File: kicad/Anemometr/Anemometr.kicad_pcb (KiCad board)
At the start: 2 copper layers, 31.8 x 26.7 mm, 74 parts, among them J1 Conn_01x01_Female, J10 Z3, J11 Z3, J12 Z4, J13 Z4, J14 SWD, J15 SWC, J16 +12v, J17 GND, J2 Conn_01x01_Female, J3 RST, J4 TxD, J5 RxD, J6 Z1, J7 Z1, J8 Z2, J9 Z2, U1 TS5A3166DBVR, U2 LMV7239, U3 TS5A3166DBVR, U4 TS5A3166DBVR, U5 STM32F103C8Tx, U6 TS5A3166DBVR, U7 LM2734Y, U8 MCP1700-5002E_SOT23, U9 MCP1700-3002E_SOT23, Y1 8MHz

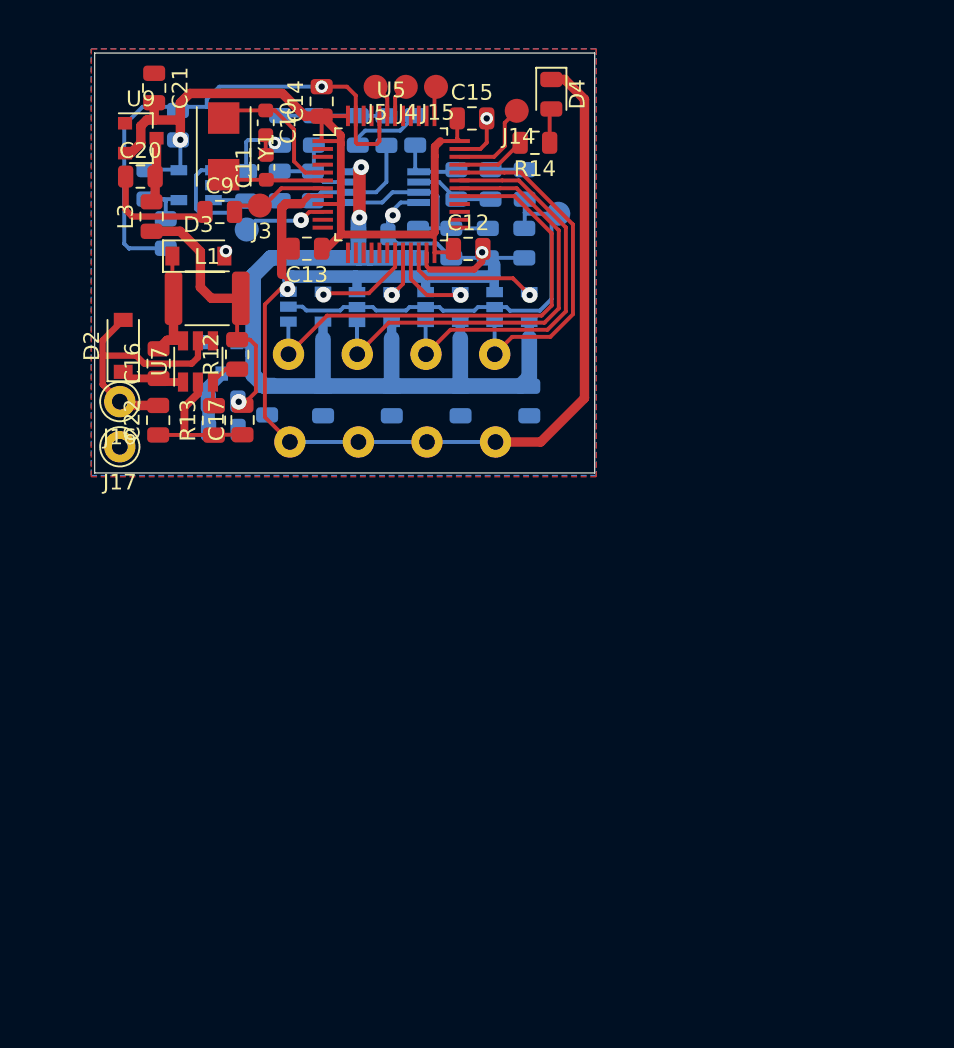
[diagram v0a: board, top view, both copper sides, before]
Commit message: изменено:      kicad/Anemometr/Anemometr-cache.lib 	изменено:      kicad/Anemometr/Anemometr.kicad_pcb 	изменено:      kicad/Anemometr/Anemometr.kicad_pcb-bak 	изменено:      kicad/Anemometr/Anemometr.sch 	изменено:      kicad/Anemometr/Anemometr.sch-bak 	изменено:      kicad/Anemometr/fp-info-cache
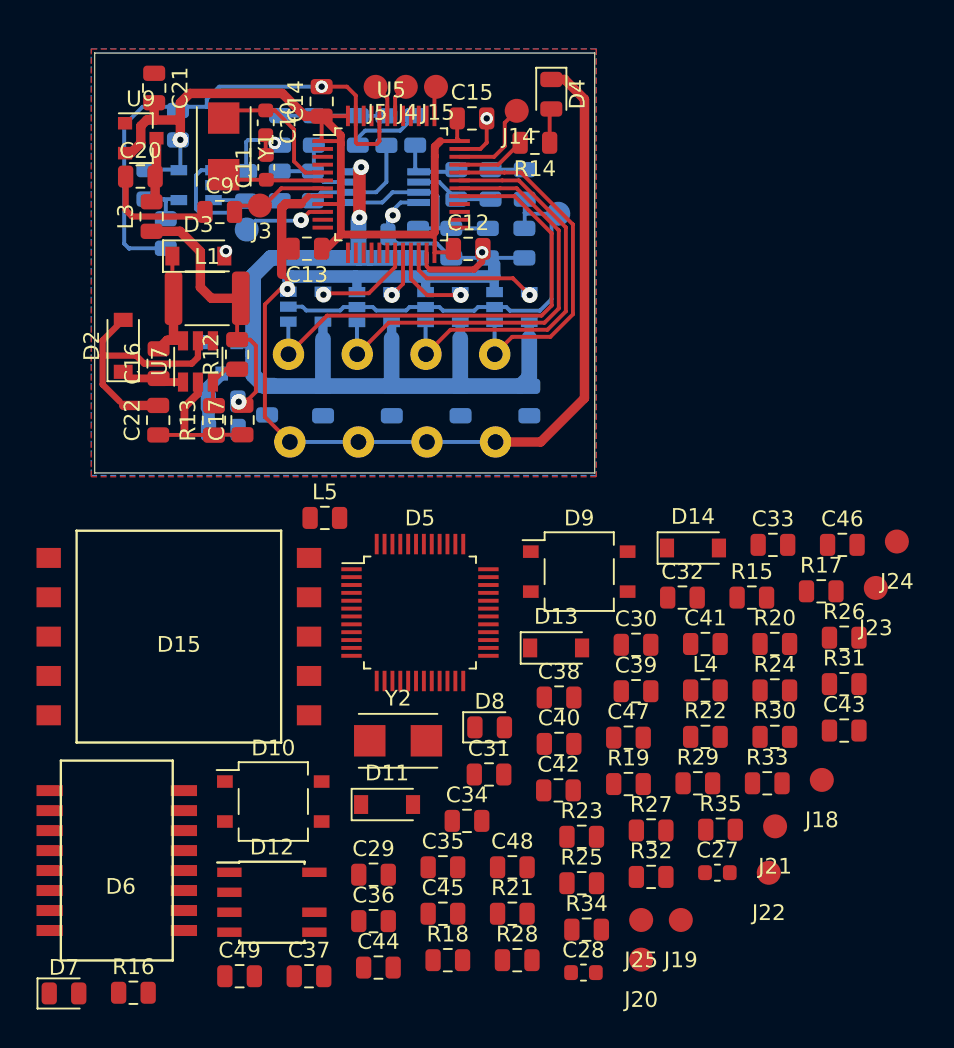
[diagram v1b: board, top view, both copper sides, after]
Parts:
- removed J16: +12v, Connector_Pin:Pin_D1.0mm_L10.0mm
- removed J17: GND, Connector_Pin:Pin_D1.0mm_L10.0mm
- added C27: 10p, Capacitor_SMD:C_0603_1608Metric, F.Cu at (62.4, 113.0)
- added C28: 10p, Capacitor_SMD:C_0603_1608Metric, F.Cu at (53.9, 119.4)
- added C29: 10uF, Capacitor_SMD:C_0805_2012Metric, F.Cu at (40.6, 113.2)
- added C30: 10uF, Capacitor_SMD:C_0805_2012Metric, F.Cu at (57.3, 98.5)
- added C31: 10nF, Capacitor_SMD:C_0805_2012Metric, F.Cu at (47.9, 106.8)
- added C32: 22nF, Capacitor_SMD:C_0805_2012Metric, F.Cu at (60.2, 95.5)
- added C33: 6.8nF, Capacitor_SMD:C_0805_2012Metric, F.Cu at (66.0, 92.2)
- added C34: 6.8nF, Capacitor_SMD:C_0805_2012Metric, F.Cu at (46.5, 109.7)
- added C35: 4.7nF/2kV, Capacitor_SMD:C_0805_2012Metric, F.Cu at (45.0, 112.7)
- added C36: 0.1uF, Capacitor_SMD:C_0805_2012Metric, F.Cu at (40.6, 116.1)
- added C37: 10uF, Capacitor_SMD:C_0805_2012Metric, F.Cu at (36.5, 119.6)
- added C38: 0.1uF, Capacitor_SMD:C_0805_2012Metric, F.Cu at (52.4, 101.9)
- added C39: 0.1uF, Capacitor_SMD:C_0805_2012Metric, F.Cu at (57.3, 101.5)
- added C40: 0.1uF, Capacitor_SMD:C_0805_2012Metric, F.Cu at (52.4, 104.8)
- added C41: 0.1uF, Capacitor_SMD:C_0805_2012Metric, F.Cu at (61.7, 98.5)
- added C42: 0.1uF, Capacitor_SMD:C_0805_2012Metric, F.Cu at (52.3, 107.8)
- added C43: 0.1uF, Capacitor_SMD:C_0805_2012Metric, F.Cu at (70.5, 104.0)
- added C44: 10uF, Capacitor_SMD:C_0805_2012Metric, F.Cu at (40.9, 119.1)
- added C45: 6.8nF, Capacitor_SMD:C_0805_2012Metric, F.Cu at (45.0, 115.6)
- added C46: 6.8nF, Capacitor_SMD:C_0805_2012Metric, F.Cu at (70.4, 92.2)
- added C47: 6.8nF, Capacitor_SMD:C_0805_2012Metric, F.Cu at (56.8, 104.5)
- added C48: 6.8nF, Capacitor_SMD:C_0805_2012Metric, F.Cu at (49.4, 112.7)
- added C49: 6.8nF, Capacitor_SMD:C_0805_2012Metric, F.Cu at (32.1, 119.6)
- added D10: MB6S, Package_TO_SOT_SMD:TO-269AA, F.Cu at (34.2, 108.5)
- added D11: MBR0540, Diode_SMD:D_SOD-123, F.Cu at (41.4, 108.7)
- added D12: SD4932B, Package_SO:SOIC-8-N7_3.9x4.9mm_P1.27mm, F.Cu at (34.1, 114.9)
- added D13: MBR0540, Diode_SMD:D_SOD-123, F.Cu at (52.2, 98.8)
- added D14: MBR0540, Diode_SMD:D_SOD-123, F.Cu at (60.9, 92.4)
- added D15: DA2257, My-library:DA2257, F.Cu at (28.2, 98.0)
- added D5: W5500, Package_QFP:LQFP-48_7x7mm_P0.5mm, F.Cu at (43.5, 96.5)
- added D6: H1102NL, My-library:H1102N, F.Cu at (24.3, 112.3)
- added D7: LED, LED_SMD:LED_0805_2012Metric, F.Cu at (20.9, 120.7)
- added D8: LED, LED_SMD:LED_0805_2012Metric, F.Cu at (48.0, 103.8)
- added D9: MB6S, Package_TO_SOT_SMD:TO-269AA, F.Cu at (53.7, 93.9)
- added J18: 1, My-library:SMD-CONN, F.Cu at (69.1, 107.1)
- added J19: 2, My-library:SMD-CONN, F.Cu at (60.1, 116.0)
- added J20: 3, My-library:SMD-CONN, F.Cu at (57.6, 118.6)
- added J21: 4, My-library:SMD-CONN, F.Cu at (66.1, 110.1)
- added J22: 5, My-library:SMD-CONN, F.Cu at (65.7, 113.0)
- added J23: 6, My-library:SMD-CONN, F.Cu at (72.5, 94.9)
- added J24: 7, My-library:SMD-CONN, F.Cu at (73.8, 92.0)
- added J25: 8, My-library:SMD-CONN, F.Cu at (57.6, 116.0)
- added L4: 47uH, Inductor_SMD:L_0805_2012Metric, F.Cu at (61.7, 101.5)
- added L5: 47uH, Inductor_SMD:L_0805_2012Metric, F.Cu at (37.5, 90.5)
- added R15: 10k, Resistor_SMD:R_0805_2012Metric, F.Cu at (64.6, 95.5)
- added R16: 82R, Resistor_SMD:R_0805_2012Metric, F.Cu at (25.3, 120.7)
- added R17: 49R9, Resistor_SMD:R_0805_2012Metric, F.Cu at (69.0, 95.2)
- added R18: 82R, Resistor_SMD:R_0805_2012Metric, F.Cu at (45.3, 118.6)
- added R19: 49R9, Resistor_SMD:R_0805_2012Metric, F.Cu at (56.8, 107.4)
- added R20: 10R, Resistor_SMD:R_0805_2012Metric, F.Cu at (66.1, 98.5)
- added R21: 75R, Resistor_SMD:R_0805_2012Metric, F.Cu at (49.4, 115.6)
- added R22: 75R, Resistor_SMD:R_0805_2012Metric, F.Cu at (61.7, 104.4)
- added R23: 150R, Resistor_SMD:R_0805_2012Metric, F.Cu at (53.8, 110.8)
- added R24: 150R, Resistor_SMD:R_0805_2012Metric, F.Cu at (66.1, 101.5)
- added R25: 1k, Resistor_SMD:R_0805_2012Metric, F.Cu at (53.8, 113.7)
- added R26: 1k, Resistor_SMD:R_0805_2012Metric, F.Cu at (70.5, 98.1)
- added R27: 1M, Resistor_SMD:R_0805_2012Metric, F.Cu at (58.2, 110.3)
- added R28: 150R, Resistor_SMD:R_0805_2012Metric, F.Cu at (49.7, 118.6)
- added R29: 150R, Resistor_SMD:R_0805_2012Metric, F.Cu at (61.2, 107.3)
- added R30: 150R, Resistor_SMD:R_0805_2012Metric, F.Cu at (66.1, 104.4)
- added R31: 150R, Resistor_SMD:R_0805_2012Metric, F.Cu at (70.5, 101.0)
- added R32: 150R, Resistor_SMD:R_0805_2012Metric, F.Cu at (58.2, 113.3)
- added R33: 150R, Resistor_SMD:R_0805_2012Metric, F.Cu at (65.6, 107.3)
- added R34: 150R, Resistor_SMD:R_0805_2012Metric, F.Cu at (54.1, 116.7)
- added R35: 150R, Resistor_SMD:R_0805_2012Metric, F.Cu at (62.6, 110.3)
- added Y2: 25MHz, Crystal:Crystal_SMD_Qantek_QC5CB-2Pin_5x3.2mm, F.Cu at (42.1, 104.7)
- R4: value 3M -> 100k
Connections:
- net SensorOut renamed SensorInput
- U5 pad 25: (no net) -> Net-(D5-Pad32)
- U5 pad 26: (no net) -> Net-(D5-Pad33)
- U5 pad 27: (no net) -> Net-(D5-Pad34)
- U5 pad 28: (no net) -> Net-(D5-Pad35)
- U5 pad 39: (no net) -> Net-(D5-Pad36)
- U5 pad 40: (no net) -> Net-(D5-Pad37)

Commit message: изменено:      kicad/Anemometr/Anemometr-cache.lib 	изменено:      kicad/Anemometr/Anemometr-rescue.lib 	изменено:      kicad/Anemometr/Anemometr.kicad_pcb 	изменено:      kicad/Anemometr/Anemometr.kicad_pcb-bak 	изменено:      kicad/Anemometr/Anemometr.sch 	изменено:      kicad/Anemometr/Anemometr.sch-bak 	изменено:      kicad/Anemometr/fp-info-cache
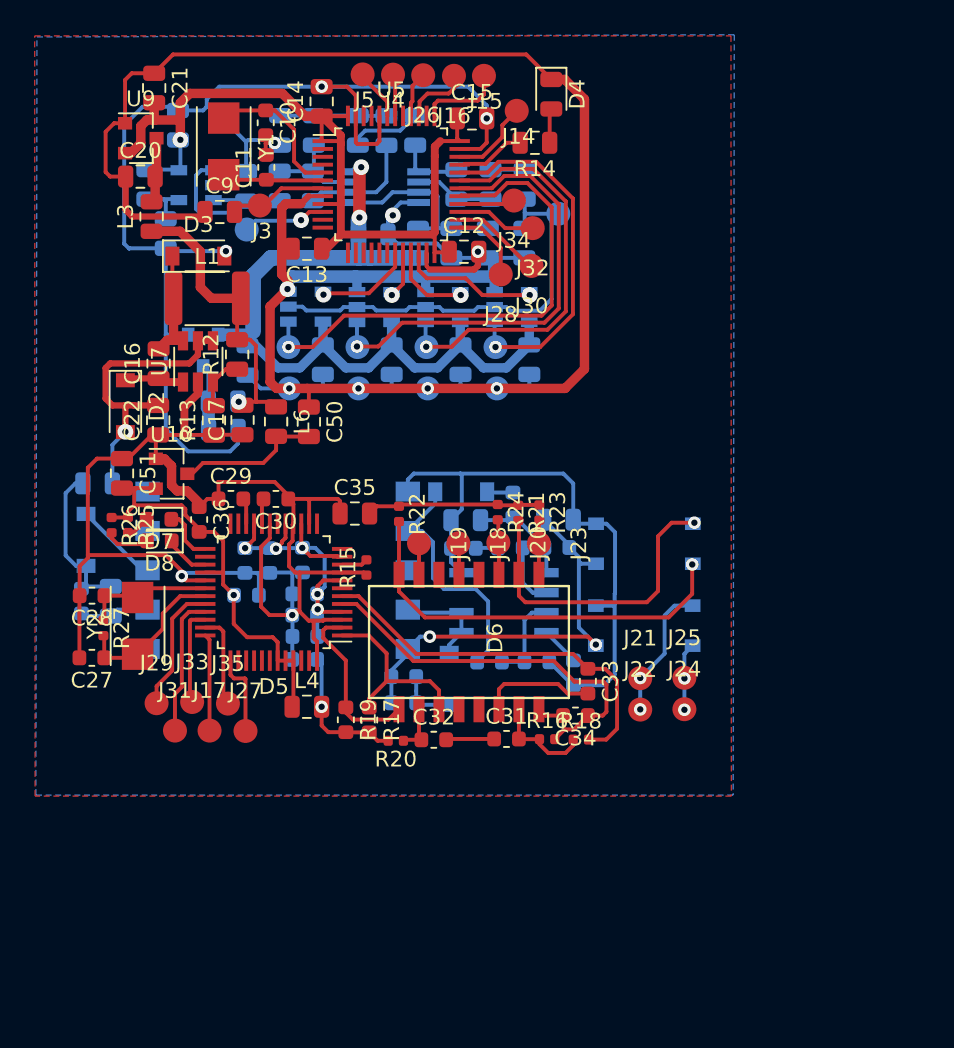
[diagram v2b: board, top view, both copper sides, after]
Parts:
- added C50: 10uF, Capacitor_SMD:C_0805_2012Metric, F.Cu at (36.5, 84.4)
- added C51: 10uF, Capacitor_SMD:C_0805_2012Metric, F.Cu at (24.6, 87.7)
- added J16: Z4, My-library:SMD-CONN, F.Cu at (45.7, 62.4)
- added J17: Z4, My-library:SMD-CONN, F.Cu at (30.2, 104.0)
- added J26: Z4, My-library:SMD-CONN, F.Cu at (43.7, 62.4)
- added J27: Z4, My-library:SMD-CONN, F.Cu at (32.4, 104.0)
- added J28: Z4, My-library:SMD-CONN, F.Cu at (48.7, 75.0)
- added J29: Z4, My-library:SMD-CONN, F.Cu at (26.8, 102.3)
- added J30: Z4, My-library:SMD-CONN, F.Cu at (50.6, 74.5)
- added J31: Z4, My-library:SMD-CONN, F.Cu at (28.0, 104.0)
- added J32: Z4, My-library:SMD-CONN, F.Cu at (50.7, 72.1)
- added J33: Z4, My-library:SMD-CONN, F.Cu at (29.1, 102.2)
- added J34: Z4, My-library:SMD-CONN, F.Cu at (49.5, 70.3)
- added J35: Z4, My-library:SMD-CONN, F.Cu at (31.3, 102.3)
- added L6: 47uH, Inductor_SMD:L_0805_2012Metric, F.Cu at (34.4, 84.4)
- added U10: MCP1700-3002E, Package_TO_SOT_SMD:SOT-23, F.Cu at (27.7, 87.7)
- C29, C30, C31, C32, C33, C34, C36: footprint Capacitor_SMD:C_0805_2012Metric -> Capacitor_SMD:C_0603_1608Metric
- C37, C38, C39, C40, C41, C42, C43, C44, C47, C48: footprint Capacitor_SMD:C_0805_2012Metric -> Capacitor_SMD:C_0603_1608Metric; moved to B.Cu
- C45, C46, C49, D10, D11, D12, D13, D14, D15, D9, L5: moved to B.Cu
- D7, D8: footprint LED_SMD:LED_0805_2012Metric -> LED_SMD:LED_0603_1608Metric
- J10, J11, J12, J13, J6, J7, J8, J9: footprint Connector_Pin:Pin_D1.0mm_L10.0mm -> My-library:SMD-CONN
- R15, R16, R18, R20, R21, R22, R23, R24, R25, R26, R27: footprint Resistor_SMD:R_0805_2012Metric -> Resistor_SMD:R_0402_1005Metric
- R17, R19: footprint Resistor_SMD:R_0805_2012Metric -> Resistor_SMD:R_0603_1608Metric
- R28, R29, R30, R31, R32, R33, R34, R35: footprint Resistor_SMD:R_0805_2012Metric -> Resistor_SMD:R_0603_1608Metric; moved to B.Cu
- U8: value MCP1700-5002E_SOT23 -> MCP1700-5002E
- U9: value MCP1700-3002E_SOT23 -> MCP1700-3002E
- moved R26 47.1 mm to (23.9, 90.9), turned to 270 degrees
- moved R35 43.1 mm to (22.0, 95.8), turned to 270 degrees
- moved C27 42.0 mm to (22.7, 99.4), turned to 180 degrees
- moved C28 39.4 mm to (22.7, 95.4), turned to 180 degrees
- moved D14 38.6 mm to (22.3, 91.9), turned to 90 degrees
- moved R27 37.1 mm to (23.4, 97.5), turned to 270 degrees
- moved R25 36.7 mm to (25.0, 90.9), turned to 270 degrees
- moved C43 34.6 mm to (36.2, 99.5), turned to 180 degrees
- moved R16 30.8 mm to (51.6, 104.5)
- moved D7 30.7 mm to (26.9, 90.6), turned to 180 degrees
- moved R17 29.9 mm to (40.3, 103.3), turned to 270 degrees
- moved J19 29.2 mm to (43.5, 92.1), turned to 90 degrees
- moved J20 28.0 mm to (48.5, 92.1), turned to 90 degrees
- moved C36 27.8 mm to (29.5, 90.6), turned to 270 degrees
- moved J18 27.6 mm to (46.0, 92.1), turned to 90 degrees
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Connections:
- C36 pad 2: +3V3 -> +3.3VDAC
- C37 pad 2: +3V3 -> +3.3VDAC
- D12 pad 8: (no net) -> Net-(C45-Pad2)
- D5 pad 28: +3V3 -> +3.3VDAC
- D5 pad 43: +3V3 -> +3.3VDAC
- D5 pad 44: +3V3 -> +3.3VDAC
- D5 pad 45: +3V3 -> +3.3VDAC
- L4 pad 1: +3V3 -> +3.3VDAC
- R25 pad 1: +3V3 -> +3.3VDAC
- R26 pad 1: +3V3 -> +3.3VDAC
- U5 pad 25: Net-(D5-Pad32) -> Net-(J28-Pad1)
- U5 pad 26: Net-(D5-Pad33) -> Net-(J30-Pad1)
- U5 pad 27: Net-(D5-Pad34) -> Net-(J32-Pad1)
- U5 pad 28: Net-(D5-Pad35) -> Net-(J34-Pad1)
- U5 pad 39: Net-(D5-Pad36) -> Net-(J16-Pad1)
- U5 pad 40: Net-(D5-Pad37) -> Net-(J26-Pad1)
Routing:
- net GND: track 157.9 -> 345.1 mm, vias 7 -> 13
- net Net-(C45-Pad2): track 0.00 -> 40.2 mm
- net +3.3VA: track 0.00 -> 33.7 mm, vias 0 -> 6
- net Net-(C45-Pad1): track 0.00 -> 27.5 mm, vias 0 -> 2
- net +3.3VDAC: track 0.00 -> 27.3 mm, vias 0 -> 1
- net Net-(D6-Pad15): track 0.00 -> 26.2 mm, vias 0 -> 1
- net Net-(C33-Pad1): track 0.00 -> 24.8 mm
- net Net-(C34-Pad1): track 0.00 -> 24.6 mm
- net Net-(D6-Pad10): track 0.00 -> 20.3 mm, vias 0 -> 1
- net Net-(D11-Pad2): track 0.00 -> 15.6 mm
- net Net-(D5-Pad1): track 0.00 -> 12.0 mm
- net Net-(C35-Pad2): track 0.00 -> 11.1 mm
- net Net-(D5-Pad2): track 0.00 -> 10.9 mm
- net Net-(C49-Pad1): track 0.00 -> 10.4 mm
- net Net-(C27-Pad1): track 0.00 -> 10.1 mm
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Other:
- board outline removed

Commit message: изменено:      kicad/Anemometr/Anemometr.kicad_pcb 	изменено:      kicad/Anemometr/Anemometr.kicad_pcb-bak 	изменено:      kicad/Anemometr/Anemometr.sch 	изменено:      kicad/Anemometr/Anemometr.sch-bak
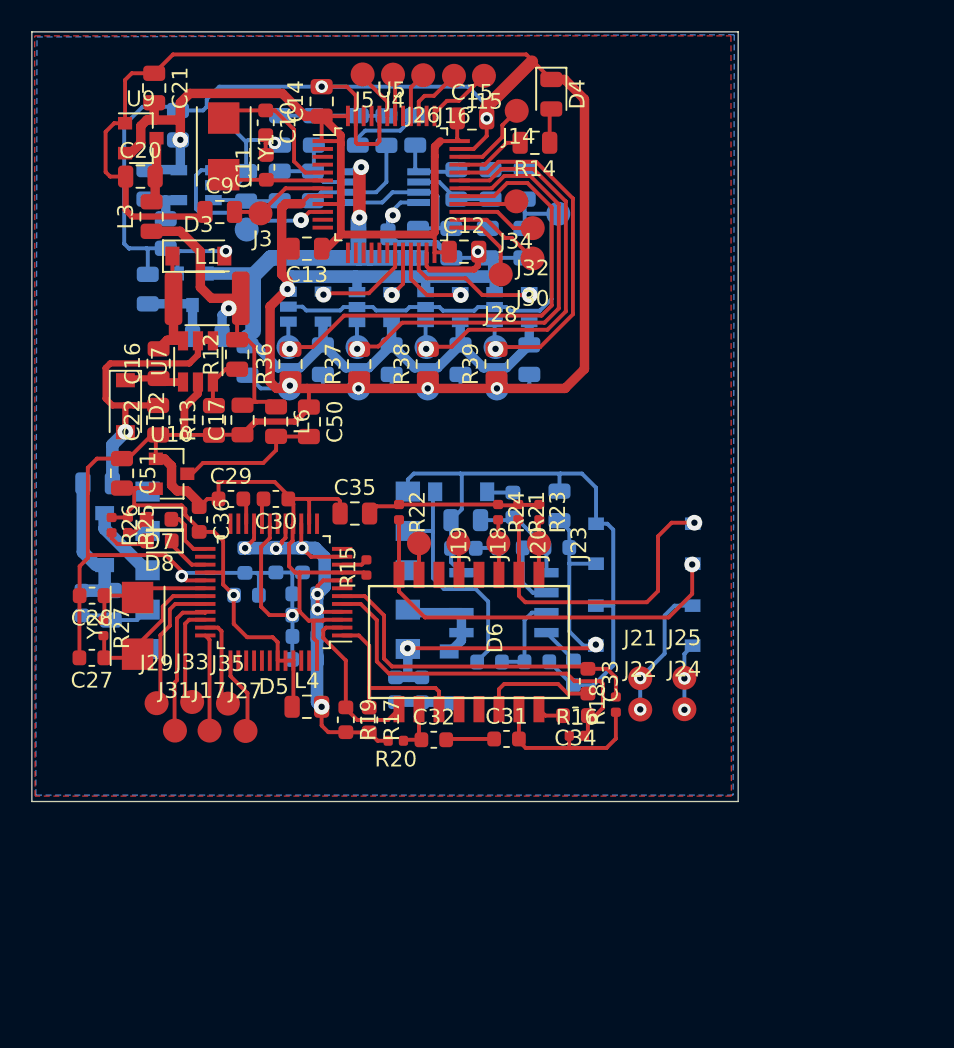
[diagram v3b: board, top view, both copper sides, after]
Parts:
- added R36: 10k, Resistor_SMD:R_0805_2012Metric, F.Cu at (35.3, 80.7)
- added R37: 10k, Resistor_SMD:R_0805_2012Metric, F.Cu at (39.7, 80.7)
- added R38: 10k, Resistor_SMD:R_0805_2012Metric, F.Cu at (44.0, 80.7)
- added R39: 10k, Resistor_SMD:R_0805_2012Metric, F.Cu at (48.4, 80.7)
- C45, C46: value 6.8nF -> 10uF/100v
- C49: value 6.8nF -> 20uF
- J10: value Z3 -> +Z3
- J11: value Z3 -> -Z3
- J12: value Z4 -> +Z4
- J13: value Z4 -> -Z4
- J6: value Z1 -> +Z1
- J7: value Z1 -> -Z1
- J8: value Z2 -> +Z2
- J9: value Z2 -> -Z2
- R35: value 150R -> 2k
- moved C18 10.1 mm to (26.2, 75.9), turned to 270 degrees
- moved L2 4.27 mm to (30.0, 78.9)
- moved U8 3.94 mm to (29.1, 76.0)
- moved R18 3.14 mm to (56.0, 102.3), turned to 90 degrees
- moved R16 1.90 mm to (53.5, 104.3)
- moved C48 1.42 mm to (43.6, 101.4), turned to 270 degrees
- moved D14 1.18 mm to (23.5, 91.8)
- moved R34 0.98 mm to (42.0, 101.4), turned to 270 degrees
- moved C45 0.88 mm to (52.4, 89.7), turned to 90 degrees
- moved J3 0.50 mm to (33.4, 71.1)
- moved J30 0.47 mm to (50.7, 74.0)
- moved C39 0.39 mm to (34.4, 93.2)
- moved C49 0.25 mm to (23.9, 96.0)
- moved J34 0.16 mm to (49.7, 70.4)
- moved R35 0.13 mm to (22.1, 95.9)
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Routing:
- net GND: track 345.1 -> 338.8 mm
- net Net-(C31-Pad2): track 6.46 -> 11.1 mm
- net Net-(C17-Pad2): track 18.9 -> 21.8 mm
- net Net-(C33-Pad1): track 24.8 -> 22.4 mm
- net Net-(J15-Pad1): track 5.33 -> 4.29 mm
- net +5VA: track 52.1 -> 53.1 mm
- net Net-(C45-Pad1): track 27.5 -> 26.8 mm
- net Net-(C49-Pad1): track 10.4 -> 9.70 mm
- net Net-(C18-Pad2): track 4.18 -> 4.85 mm
- net Net-(D14-Pad2): track 5.39 -> 4.81 mm
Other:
- board outline added: 44.9 x 48.9 mm
